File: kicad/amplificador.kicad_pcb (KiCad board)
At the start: 2 copper layers, 202 x 103 mm, 86 parts, among them J1 Screw_Terminal_01x01, J10 Conn_01x01_Male, J11 Conn_01x01_Male, J12 Conn_01x01_Male, J13 Conn_01x01_Male, J14 Screw_Terminal_01x01, J15 Conn_01x01_Male, J16 Screw_Terminal_01x01, J17 Screw_Terminal_01x01, J18 Conn_01x01_Male, J19 Conn_01x01_Male, J2 Conn_01x01_Male, J20 Conn_01x01_Male, J21 Screw_Terminal_01x01, J22 Screw_Terminal_01x01, J23 Screw_Terminal_01x01, J24 Screw_Terminal_01x01, J3 Conn_01x01_Male, J4 Conn_01x01_Male, J5 Conn_01x01_Male, J6 Conn_01x01_Male, J7 Screw_Terminal_01x01, J8 Screw_Terminal_01x01, J9 Conn_01x01_Male, Q1 MPSA92, Q10 MPSA42, Q11 BD135, Q12 BD136, Q13 BD135, Q14 BD136, Q15 2SD1047, Q16 2SD1047, Q17 2SB817, Q18 2SB817, Q2 MPSA42, Q3 MPSA92, Q4 MPSA42, Q5 MPSA92, Q6 MPSA92, Q7 MPSA42, Q8 MPSA92, Q9 BD135, U1 LM385D-1.2, U2 LM385D-1.2

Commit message: actualizamos lista de materiales y algunos valores del circuito que estaban mal
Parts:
- R1: value 400 -> 12k
- R18: value 16 -> 10
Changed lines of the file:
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@@
       (effects (font (size 1 1) (thickness 0.15)))
     )
-    (fp_text value 400 (at 0 1.65) (layer F.Fab)
+    (fp_text value 12k (at 0 1.65) (layer F.Fab)
       (effects (font (size 1 1) (thickness 0.15)))
     )
@@
       (effects (font (size 1 1) (thickness 0.15)))
     )
-    (fp_text value 16 (at 0 1.65) (layer F.Fab)
-      (effects (font (size 1 1) (thickness 0.15)))
-    )
+    (fp_text value 10 (at 0 1.65) (layer F.Fab)
+      (effects (font (size 1 1) (thickness 0.15)))
+    )

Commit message: el jumper JP4 estaba mal, tenía que ir a tierra, se actualizó el esquemático y el pcb. En el pcb se saco una via
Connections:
- JP4 pad 1: Net-(C4-Pad1) -> GND
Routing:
- net Net-(C4-Pad1): track 22.2 -> 13.3 mm, vias 1 -> 0
- net GND: track 191.3 -> 193.3 mm
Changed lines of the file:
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@@
     (thickness 1.6)
     (drawings 4)
-    (tracks 498)
+    (tracks 496)
     (zones 0)
     (modules 86)
@@
       (net 45 /Io2))
     (pad 1 thru_hole rect (at 0 0 90) (size 1.7 1.7) (drill 1) (layers *.Cu *.Mask)
-      (net 4 "Net-(C4-Pad1)"))
+      (net 3 GND))
     (model ${KISYS3DMOD}/Connector_PinHeader_2.54mm.3dshapes/PinHeader_1x02_P2.54mm_Vertical.wrl
       (at (xyz 0 0 0))
@@
   (segment (start 115.54353 60.8222) (end 114.781528 61.584202) (width 0.7874) (layer F.Cu) (net 3))
   (segment (start 116.6749 60.8222) (end 115.54353 60.8222) (width 0.7874) (layer F.Cu) (net 3))
+  (segment (start 184.912 120.65) (end 184.912 122.682) (width 0.7874) (layer B.Cu) (net 3))
   (segment (start 176.5427 115.9256) (end 176.5427 119.3673) (width 0.7874) (layer F.Cu) (net 4))
   (segment (start 176.4171 115.8) (end 176.5427 115.9256) (width 0.7874) (layer F.Cu) (net 4))
   (segment (start 168.91 115.8) (end 176.4171 115.8) (width 0.7874) (layer F.Cu) (net 4))
   (segment (start 176.5427 119.3673) (end 176.5427 121.4956) (width 0.7874) (layer F.Cu) (net 4))
-  (via (at 176.5427 119.3673) (size 1.309624) (drill 0.700024) (layers F.Cu B.Cu) (net 4))
-  (segment (start 177.8254 120.65) (end 176.5427 119.3673) (width 0.7874) (layer B.Cu) (net 4))
-  (segment (start 184.912 120.65) (end 177.8254 120.65) (width 0.7874) (layer B.Cu) (net 4))
   (segment (start 198.3576 84.2698) (end 199.4826 85.3948) (width 0.7874) (layer F.Cu) (net 5))
   (segment (start 188.75988 84.2698) (end 198.3576 84.2698) (width 0.7874) (layer F.Cu) (net 5))

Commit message: cambiamos resistencia de 200 por una de 220
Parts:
- R23: value 200 -> 220
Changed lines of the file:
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@@
       (effects (font (size 1 1) (thickness 0.15)))
     )
-    (fp_text value 200 (at 0 1.65 90) (layer F.Fab)
+    (fp_text value 220 (at 0 1.65 90) (layer F.Fab)
       (effects (font (size 1 1) (thickness 0.15)))
     )

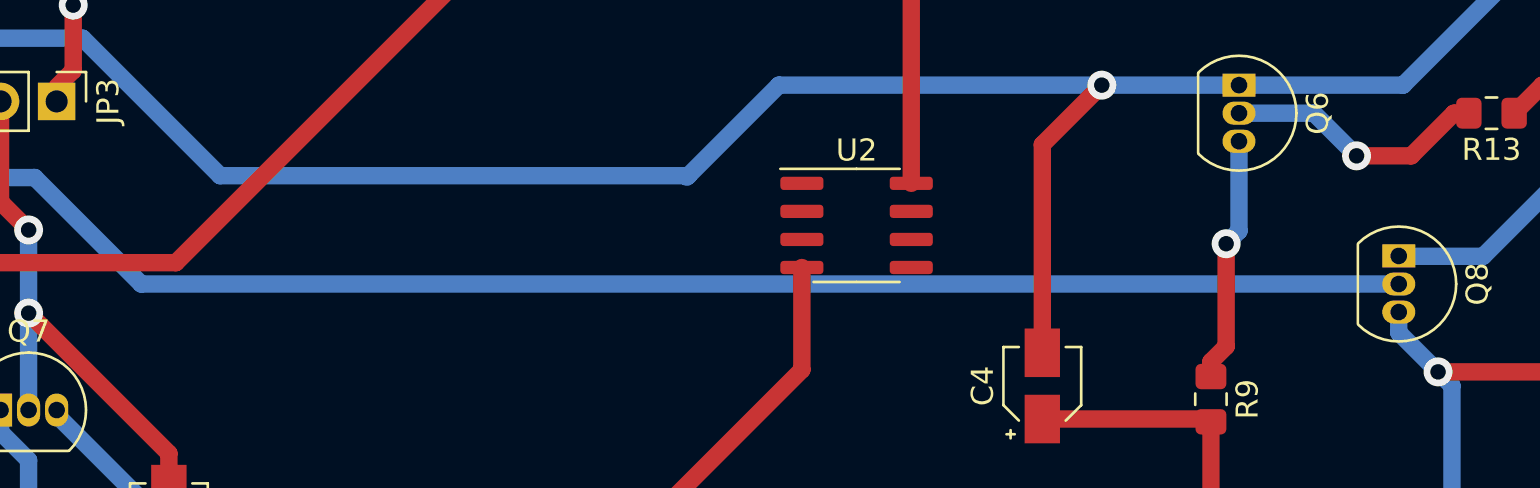
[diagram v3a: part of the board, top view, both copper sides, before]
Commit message: corregimos la conexió que faltaba en la fuente de corriente en el proyecto de kicad
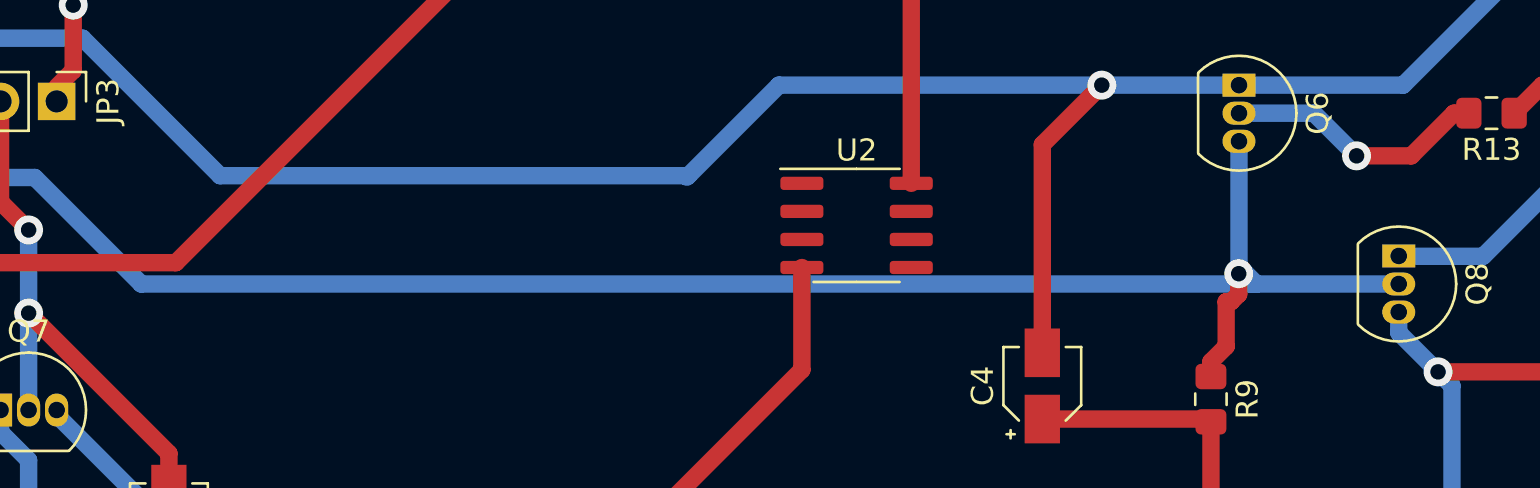
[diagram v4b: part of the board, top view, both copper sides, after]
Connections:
- Q8 pad 2: Net-(Q8-Pad2) -> Net-(Q6-Pad3)
- R7 pad 2: Net-(Q8-Pad2) -> Net-(Q6-Pad3)
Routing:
- net Net-(Q6-Pad3): track 11.3 -> 108.7 mm, vias 1 -> 2
- net Net-(Q8-Pad2): track 96.0 -> 0.00 mm, vias 1 -> 0

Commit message: Etapa VAS bien polarizada.
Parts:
- moved U2 0.36 mm to (160.5, 106.7), turned to 180 degrees
- turned U1 to 0 degrees
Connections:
- U1 pad 4: Net-(R16-Pad1) -> /Io2
- U1 pad 8: /Io2 -> Net-(R16-Pad1)
- U2 pad 4: /Vo_vas -> Net-(C6-Pad1)
- U2 pad 8: Net-(C6-Pad1) -> /Vo_vas

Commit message: trabajo del 13/03
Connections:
- D3 pad 1: Net-(D3-Pad1) -> /Io2
- J9 pad 1: Net-(D3-Pad1) -> Net-(J9-Pad1)
- Q8 pad 1: Net-(D3-Pad1) -> Net-(J9-Pad1)
- R13 pad 1: Net-(D3-Pad1) -> Net-(J9-Pad1)
- R14 pad 1: Net-(D3-Pad1) -> Net-(J9-Pad1)
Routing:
- net Net-(D3-Pad1): track 60.8 -> 0.00 mm, vias 1 -> 0
- net Net-(J9-Pad1): track 0.00 -> 53.1 mm, vias 0 -> 1
- net /Io2: track 35.3 -> 63.9 mm

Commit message: trabajo del 16/03
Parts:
- moved D3 7.49 mm to (223.5, 87.6), turned to 270 degrees
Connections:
- D3 pad 1: /Io2 -> Net-(D3-Pad1)
- D3 pad 2: Net-(D3-Pad2) -> /Io2
- Q11 pad 3: Net-(D3-Pad2) -> Net-(D3-Pad1)
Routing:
- net Net-(D3-Pad2): track 8.61 -> 0.00 mm
- net Net-(D3-Pad1): track 0.00 -> 8.61 mm
